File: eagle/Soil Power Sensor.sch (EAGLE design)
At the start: 59 parts, among them U1 INA296A5, U2 MAX9944ASA, U3 ADS1219IPWR, U4 THS4532, U5 REF2033, U6 TPS60400DBV, U7 ESP32-C3-MINI-1-N4, U8 FM24CL16B-G, U9 WIO-E5_MINI, X1 Voltage, X2 Current, X3 GND, X4 SDI

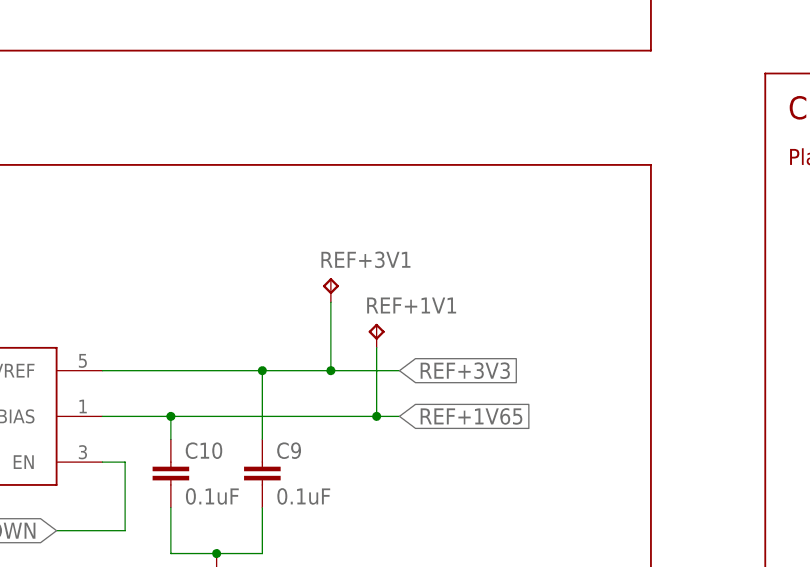
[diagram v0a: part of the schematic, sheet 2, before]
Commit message: Moved Eagle files to eagle/
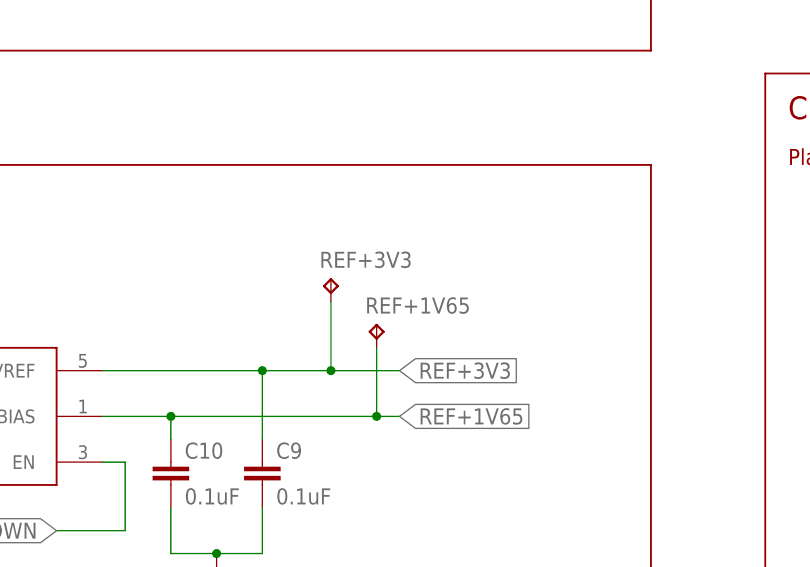
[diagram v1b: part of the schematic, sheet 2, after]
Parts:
- renumbered REF+1V1 to REF+1V65, REF+3V1 to REF+3V3
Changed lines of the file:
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@@
 <part name="VUSB" library="testpad" library_urn="urn:adsk.eagle:library:385" deviceset="TP" device="B1,27" package3d_urn="urn:adsk.eagle:package:27944/2"/>
 <part name="VCC" library="testpad" library_urn="urn:adsk.eagle:library:385" deviceset="TP" device="B1,27" package3d_urn="urn:adsk.eagle:package:27944/2"/>
-<part name="REF+1V1" library="testpad" library_urn="urn:adsk.eagle:library:385" deviceset="TP" device="B1,27" package3d_urn="urn:adsk.eagle:package:27944/2"/>
-<part name="REF+3V1" library="testpad" library_urn="urn:adsk.eagle:library:385" deviceset="TP" device="B1,27" package3d_urn="urn:adsk.eagle:package:27944/2"/>
+<part name="REF+1V65" library="testpad" library_urn="urn:adsk.eagle:library:385" deviceset="TP" device="B1,27" package3d_urn="urn:adsk.eagle:package:27944/2"/>
+<part name="REF+3V3" library="testpad" library_urn="urn:adsk.eagle:library:385" deviceset="TP" device="B1,27" package3d_urn="urn:adsk.eagle:package:27944/2"/>
 <part name="3V3" library="testpad" library_urn="urn:adsk.eagle:library:385" deviceset="TP" device="B1,27" package3d_urn="urn:adsk.eagle:package:27944/2"/>
 <part name="U2" library="Soil Power Sensor" deviceset="MAX9944" device="ASA"/>
@@
 <attribute name="TP_SIGNAL_NAME" x="97.79" y="184.15" size="1.778" layer="97"/>
 </instance>
-<instance part="REF+1V1" gate="G$1" x="104.14" y="109.22" smashed="yes">
+<instance part="REF+1V65" gate="G$1" x="104.14" y="109.22" smashed="yes">
 <attribute name="NAME" x="102.87" y="110.49" size="1.778" layer="95"/>
 <attribute name="TP_SIGNAL_NAME" x="105.41" y="107.95" size="1.778" layer="97"/>
 </instance>
-<instance part="REF+3V1" gate="G$1" x="99.06" y="114.3" smashed="yes">
+<instance part="REF+3V3" gate="G$1" x="99.06" y="114.3" smashed="yes">
 <attribute name="NAME" x="97.79" y="115.57" size="1.778" layer="95"/>
 <attribute name="TP_SIGNAL_NAME" x="100.33" y="113.03" size="1.778" layer="97"/>
@@
 <label x="106.68" y="104.14" size="1.778" layer="95" xref="yes"/>
 <wire x1="91.44" y1="104.14" x2="99.06" y2="104.14" width="0.1524" layer="91"/>
-<pinref part="REF+3V1" gate="G$1" pin="TP"/>
+<pinref part="REF+3V3" gate="G$1" pin="TP"/>
 <wire x1="99.06" y1="104.14" x2="106.68" y2="104.14" width="0.1524" layer="91"/>
 <wire x1="99.06" y1="111.76" x2="99.06" y2="104.14" width="0.1524" layer="91"/>
@@
 <junction x="81.28" y="99.06"/>
 <label x="106.68" y="99.06" size="1.778" layer="95" xref="yes"/>
-<pinref part="REF+1V1" gate="G$1" pin="TP"/>
+<pinref part="REF+1V65" gate="G$1" pin="TP"/>
 <wire x1="104.14" y1="99.06" x2="106.68" y2="99.06" width="0.1524" layer="91"/>
 <wire x1="104.14" y1="106.68" x2="104.14" y2="99.06" width="0.1524" layer="91"/>
